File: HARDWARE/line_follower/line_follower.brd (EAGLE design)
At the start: 150 x 110.3 mm, 67 parts, among them IC1 ATMEGA328PMA, IC2 LF50, IC3 L6205, IC4 L3GD20HSMD, Q1 CSM-7X-DU, T1 BPX81, T2 BPX81, T3 BPX81, T4 BPX81, T7 BPX81, T8 BPX81

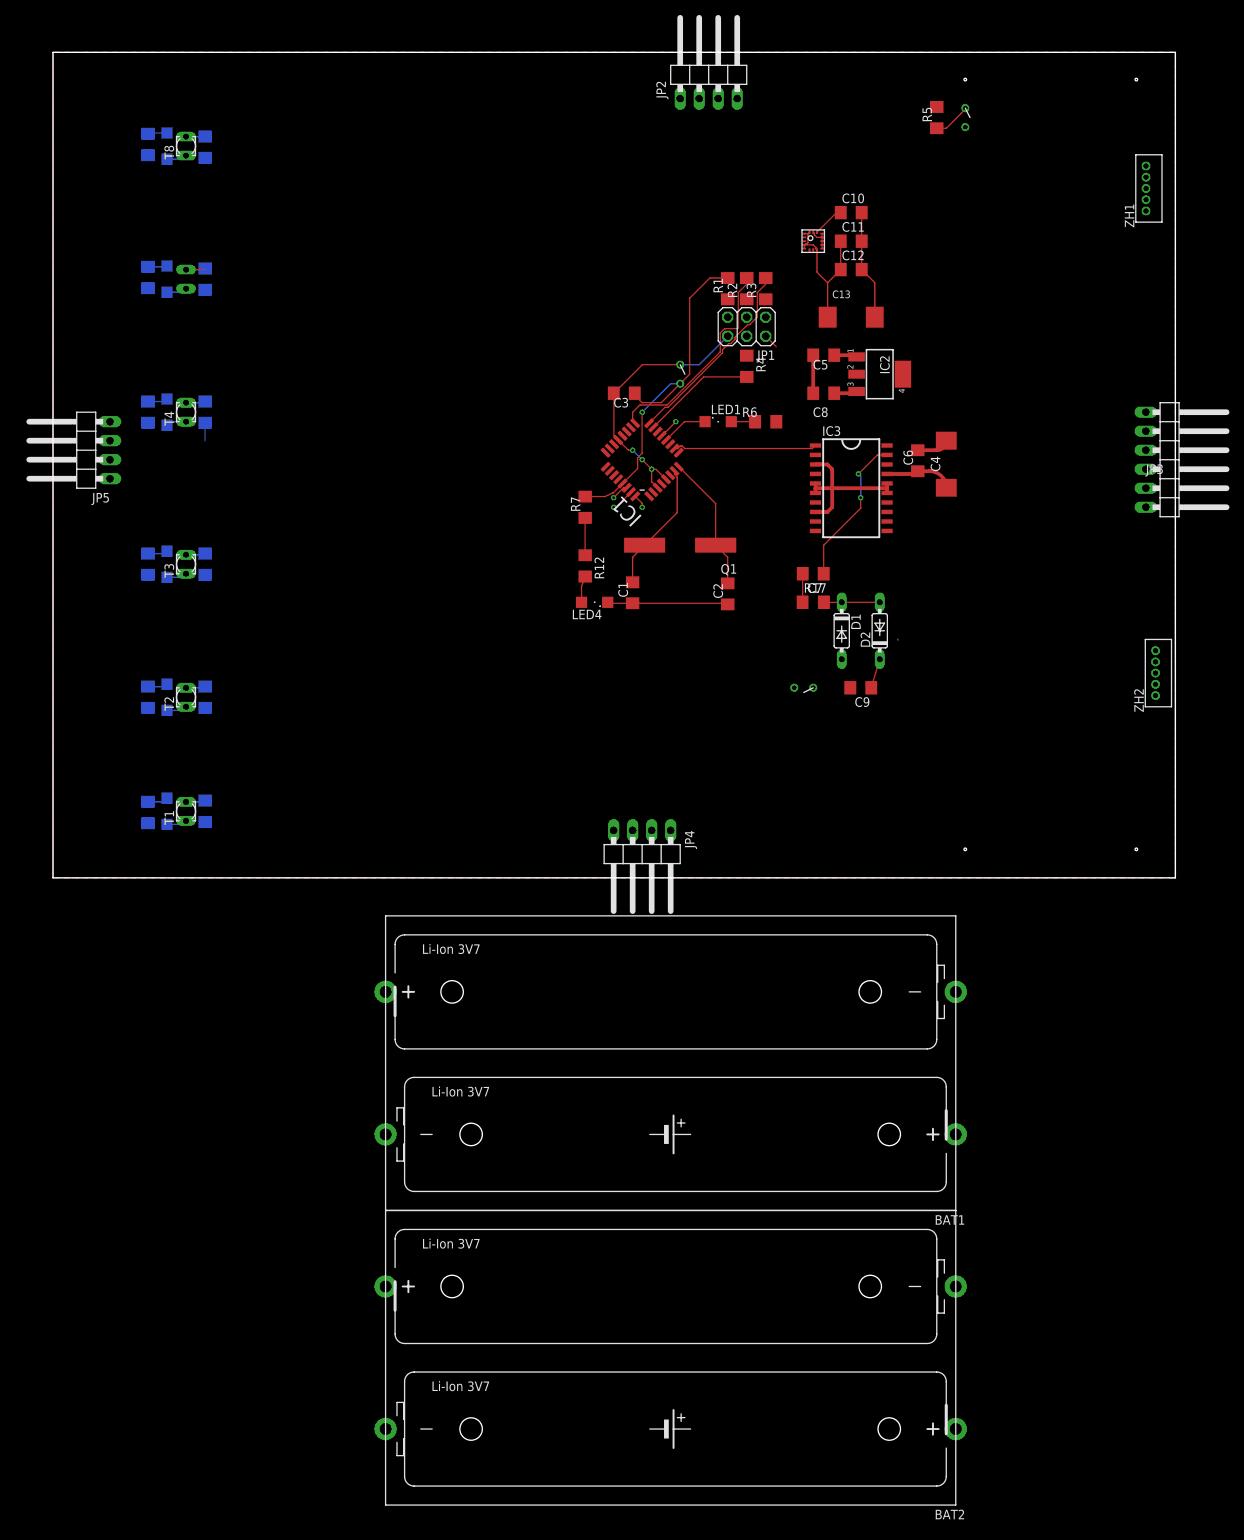
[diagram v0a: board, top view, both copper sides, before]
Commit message: finished front module
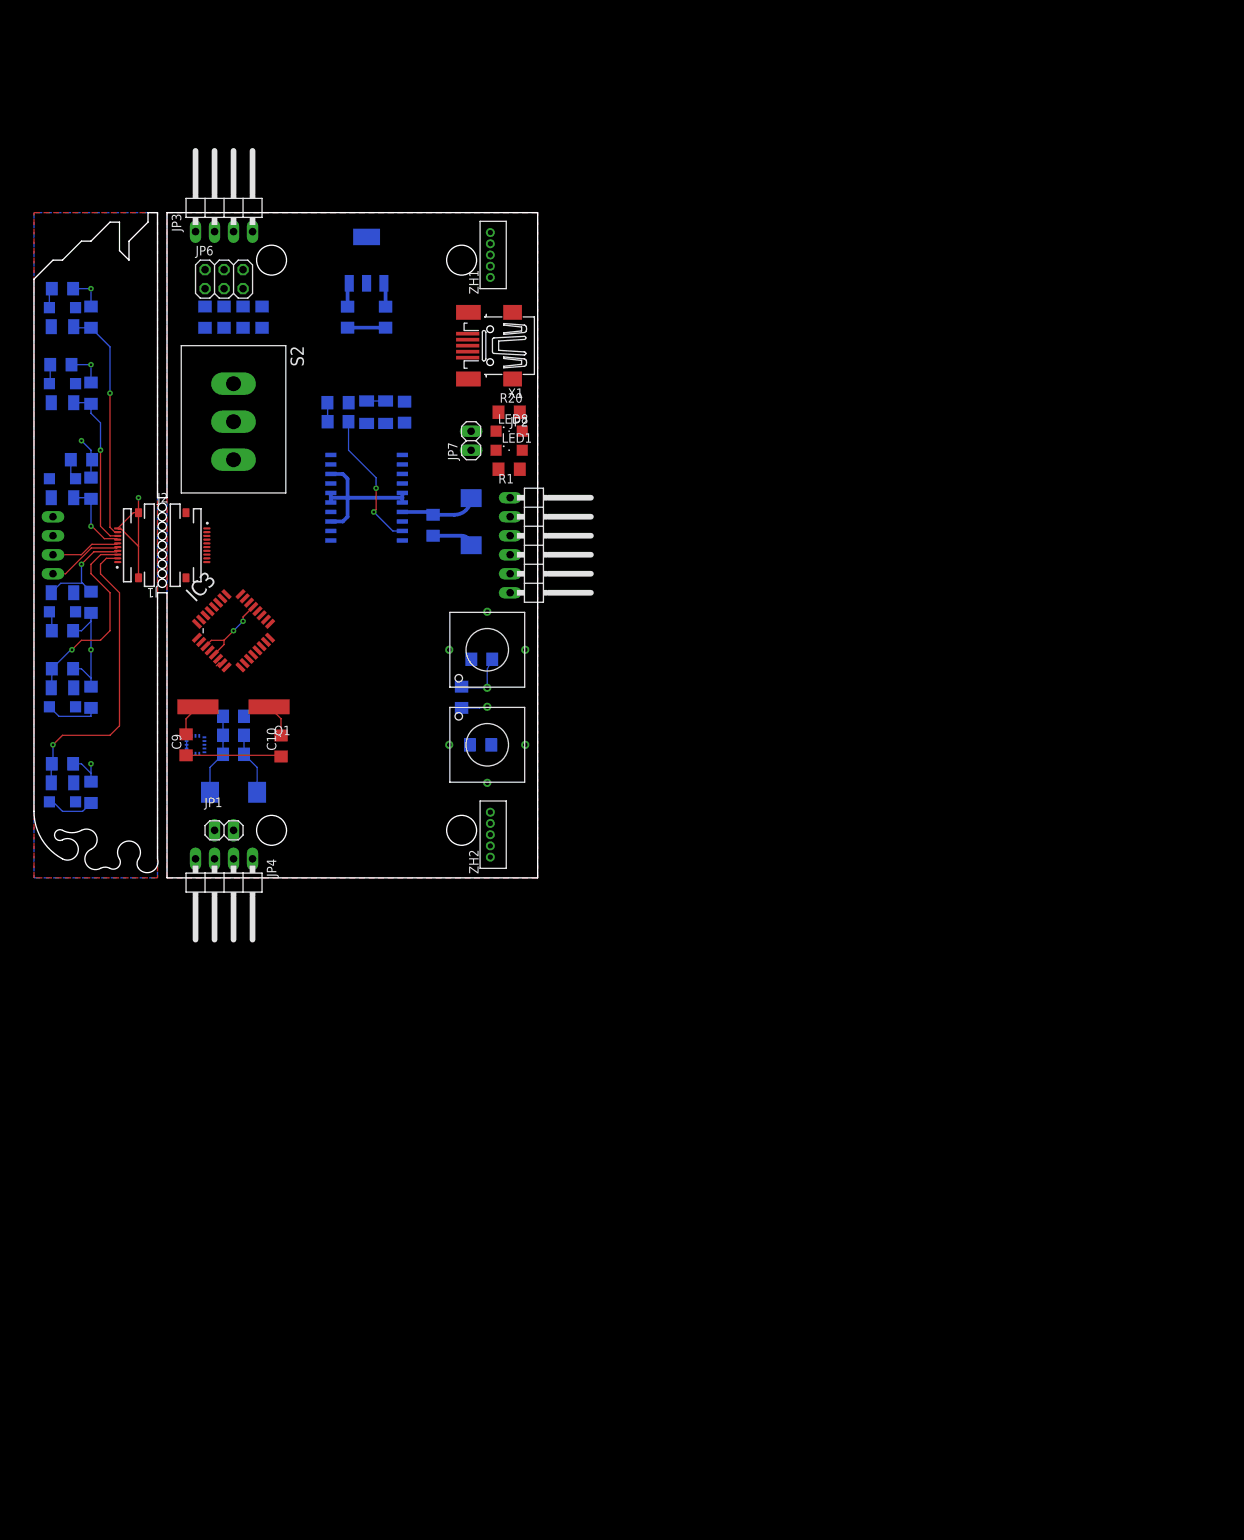
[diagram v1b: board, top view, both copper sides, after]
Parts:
- removed BAT1, BAT2: BATSERIES, martinmake:BAT2X18650SERIES
- removed LED10, LED9: White, led:SML1206
- removed R22, R24: 220, rcl:R1206
- removed R23, R25: 10k, rcl:R1206
- removed T7, T8: BPX81, opto-trans-siemens:BPX81
- removed USR: SWITCHTHT, martinmake:SWITCH
- added J1, J2: FFC2B05-10-X_REVC, FFC2B05-10-X_REVC:GCT_FFC2B05-10-X_REVC
- added JP6: ICSP, pinhead:2X03
- added JP7: 3S/4S, pinhead:1X02
- added LED7: White, led:SML1206
- added LED8: Orange, led:SML1206
- added R18, R19: 120, rcl:R1206
- added R20: 220, rcl:R1206
- added R21: 100k, rcl:R1206
- added S1: BUTTON, martinmake:BUTTON
- added T5, T6: ELPT15-21C, martinmake:1206
- added X1: MINI-USB-SCHIELD-32005-201, con-cypressindustries:32005-201
- C1: value 22p -> 10u; device rcl:C1206 -> rcl:SMC_D
- C10, C9: value 10n -> 22p
- C13: value 10u -> 100n; device rcl:SMC_D -> rcl:C1206
- C2: value 22p -> 100n
- C4: value 100u -> 10n; device rcl:SMC_D -> rcl:C1206
- C5: value 100n -> 100u; device rcl:C1206 -> rcl:SMC_D
- C8: value 100n -> 10n
- D1, D2: device diode:DO35-7 -> martinmake:1206
- IC1: value ATMEGA328PMA -> L3GD20HSMD; device martinmake:TQFP32 -> martinmake:LGA-16
- IC2: value LF50 -> L6205; device linear:SOT223 -> martinmake:SO20
- IC3: value L6205 -> ATMEGA328PMA; device martinmake:SO20 -> martinmake:TQFP32
- IC4: value L3GD20HSMD -> LF33; device martinmake:LGA-16 -> linear:SOT223
- JP1: value ICSP -> (none); device pinhead:2X03 -> pinhead:1X02
- JP2: value RDS -> UART; device pinhead:1X04/90 -> pinhead:1X06/90
- JP3: value UART -> RDS; device pinhead:1X06/90 -> pinhead:1X04/90
- LED4: value Orange -> White
- Q1: value CSM-7X-DU -> 10MHz
- R1: value 120 -> 680
- R13, R15: value 220 -> 10k
- R14: value 10k -> 220
- R16: value 10k -> 120
- R17: value 220 -> 120
- R2: value 120 -> 1k
- R3, R4: value 120 -> 220
- R5: value 1k -> 10k
- R6: value 680 -> 220
- R7: value 100k -> 10k
- S2: value SWITCHTHT -> DUALSWITCH; device martinmake:SWITCH -> martinmake:DUALSWITCH
- S3: value SWITCHTHT -> BUTTON; device martinmake:SWITCH -> martinmake:BUTTON
- T1, T2, T3, T4: value BPX81 -> ELPT15-21C; device opto-trans-siemens:BPX81 -> martinmake:1206
- moved R5 145.3 mm to (1.27, 15.2), flipped to the bottom, turned to 0 degrees
- moved JP3 131.5 mm to (22.9, 90.2), turned to 0 degrees
- moved R4 104.5 mm to (5.08, 11.4), flipped to the bottom
- moved C10 104.3 mm to (30.5, 17.6), turned to 90 degrees
- moved C4 101.0 mm to (24.1, 21.6), flipped to the bottom, turned to 0 degrees
- moved R6 97.4 mm to (5.08, 24.1), flipped to the bottom, turned to 270 degrees
- moved JP1 97.0 mm to (22.9, 6.35), turned to 0 degrees
- moved ZH2 91.5 mm to (57.1, 1.27)
- moved C9 90.5 mm to (17.8, 17.8), turned to 90 degrees
- moved ZH1 88.1 mm to (57.1, 78.7)
- moved R17 87.5 mm to (22.9, 74.9), flipped to the bottom, turned to 270 degrees
- moved IC3 84.7 mm to (24.1, 33.0), turned to 45 degrees
- moved R12 75.1 mm to (1.05, 68.6), flipped to the bottom, turned to 0 degrees
- moved R7 73.1 mm to (1.27, 27.9), flipped to the bottom, turned to 0 degrees
- moved D2 72.2 mm to (44.5, 62.2), flipped to the bottom, turned to 270 degrees
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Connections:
- removed net GND2: LED10.C, LED2.C, LED3.C, LED5.C, LED6.C, LED9.C, T1.E, T2.E, T3.E, T4.E, T7.E, T8.E
- removed net N$10: BAT1.+@1, BAT1.-@2
- removed net N$11: IC4.6
- removed net N$13: IC4.7
- removed net N$14: BAT1.+@2, S3.P$2
- removed net N$15: BAT1.-@1, BAT2.+@2
- removed net N$24: R15.1
- removed net N$32: R13.1
- removed net N$38: R22.1
- removed net N$40: R10.1
- removed net N$41: R24.1
- removed net N$45: R8.1
- removed net VM: C4.+, C5.1, C6.1, C9.2, D1.A, IC2.1, IC3.14, IC3.17, S3.P$1
- new net F_ADC0: J1.2, R5.2, T1.1
- new net F_ADC1: J1.3, R7.2, T2.1
- new net F_ADC2: J1.4, R9.2, T3.1
- new net F_ADC3: J1.7, R11.2, T4.1
- new net F_ADC6: J1.8, R13.2, T5.1
- new net F_ADC7: J1.9, R15.2, T6.1
- new net F_GND: J1.10, J1.11, J1.12, JP5.2, LED2.C, LED3.C, LED4.C, LED5.C, LED6.C, LED7.C, T1.2, T2.2, T3.2, T4.2, T5.2, T6.2
- new net F_SCL: J1.5, JP5.4
- new net F_SDA: J1.6, JP5.3
- new net F_VCC: J1.1, JP5.1, R10.1, R11.1, R12.1, R13.1, R14.1, R15.1, R4.1, R5.1, R6.1, R7.1, R8.1, R9.1
- new net N$8: IC1.7, JP1.1
- new net VB: C11.1, C5.+, C6.1, C7.2, D1.1, IC2.14, IC2.17, IC4.1, JP7.1, S2.A, S2.COM
- new net VUSB: S2.B, X1.1
- net !RESET: now also C13.1, IC3.29, R16.2, R21.2, S3.A@1, S3.A@2; no longer C3.1, IC1.29, R1.2, R7.2, S2.P$2
- net !SS: now also IC3.14; no longer IC1.14
- net ADC0: now also IC3.23, J2.2; no longer IC1.23, R9.2, T1.C
- net ADC1: now also IC3.24, J2.3; no longer IC1.24, R11.2, T2.C
- net ADC2: now also IC3.25, J2.4; no longer IC1.25, R14.2, T3.C
- net ADC3: now also IC3.26, J2.7; no longer IC1.26, R16.2, T4.C
- net ADC6: now also IC3.19, J2.8; no longer IC1.19, R23.2, T7.C
- net ADC7: now also IC3.22, J2.9; no longer IC1.22, R25.2, T8.C
- net DIRA: now also IC2.2; no longer IC1.2
- net DIRB: now also IC2.10, IC3.11; no longer IC1.11, IC3.10
- net GND: now also C1.-, C10.1, C13.2, C2.2, C4.2, C5.-, C9.1, IC1.10, IC1.11, IC1.12, IC1.13, IC1.15, IC1.9, IC2.15, IC2.16, IC2.3, IC2.5, IC2.6, IC2.8, IC3.21, IC4.4, J2.10, J2.11, J2.12, JP2.1, JP3.2, JP6.6, JP7.2, LED8.C, R2.2, S3.B@1, S3.B@2, X1.5, X1.M1, X1.M2, X1.M3, X1.M4; no longer BAT2.-@1, C1.1, C10.2, C13.-, C2.1, C4.-, C5.2, C8.2, IC1.21, IC1.3, IC1.5, IC2.4, IC3.15, IC3.16, IC3.6, IC3.8, IC4.10, IC4.11, IC4.12, IC4.13, IC4.15, IC4.9, JP1.6, JP2.2, JP3.1, JP5.2, LED4.C, R5.2, S2.P$1
- net INT0: now also IC3.32; no longer IC1.32
- net INT1: now also IC3.1; no longer IC1.1
- net LED: now also IC3.12; no longer IC1.12
- net MISO: now also IC3.16, R18.2; no longer IC1.16, R3.2
- net MOSI: now also IC3.15, R19.2; no longer IC1.15, R4.2
- net N$1: now also LED4.A, R8.2; no longer LED5.A, R13.2
- net N$12: now also LED5.A, R10.2; no longer LED6.A, R15.2
- net N$2: now also C7.1, D2.2, IC2.12; no longer C9.1, D2.C, IC3.12
- net N$22: now also LED7.A, R14.2; no longer LED10.A, R24.2
- net N$3: now also D1.2, D2.1, R3.2; no longer D1.C, D2.A, R17.2
- net N$30: now also LED6.A, R12.2; no longer LED9.A, R22.2
- net N$33: now also JP6.1, R18.1; no longer JP1.1, R3.1
- net N$36: now also LED8.A, R20.2; no longer LED4.A, R12.2
- net N$4: now also C8.2, R3.1; no longer C7.2, R17.1
- net N$43: now also R6.2; no longer R10.2
- net N$47: now also R4.2; no longer R8.2
- net N$49: now also JP6.3, R17.1; no longer JP1.3, R2.1
- net N$5: now also R1.1; no longer R6.1
- net N$50: now also JP6.5, R16.1; no longer JP1.5, R1.1
- net N$51: now also JP6.4, R19.1; no longer JP1.4, R4.1
- net N$6: now also C4.1, IC1.14; no longer C10.1, IC4.14
- net N$7: now also C8.1, IC2.19; no longer C7.1, IC3.19
- net N$9: now also IC1.6, JP1.2; no longer BAT2.+@1, BAT2.-@2
- net OC0A: now also IC2.1, IC3.10; no longer IC1.10, IC3.1
- net OC0B: now also IC2.9; no longer IC1.9
- net OUT1A: now also IC2.4; no longer IC3.4
- net OUT1B: now also IC2.7; no longer IC3.7
- net OUT2A: now also IC2.18; no longer IC3.18
- net OUT2B: now also IC2.13; no longer IC3.13
- net RX: now also IC3.30, JP2.4; no longer IC1.30, JP3.4
- net SCK: now also IC3.17, R17.2; no longer IC1.17, R2.2
- net SCL: now also IC1.2, IC3.28, J2.5, JP3.4; no longer IC1.28, IC4.2, JP2.3, JP5.4
- net SDA: now also IC1.3, IC3.27, J2.6, JP3.3; no longer IC1.27, IC4.3, JP2.4, JP5.3
- net TX: now also IC3.31, JP2.5; no longer IC1.31, JP3.5
- net USR: now also IC3.13, R2.1, S1.A@1, S1.A@2; no longer IC1.13, R5.1, USR.P$1
- net VCC: now also C1.+, C2.1, C3.1, IC1.1, IC1.16, IC1.5, IC1.8, IC2.11, IC2.20, IC3.18, IC3.4, IC3.6, IC4.3, J2.1, JP2.3, JP3.1, JP6.2, R1.2, R20.1, R21.1, S1.B@1, S1.B@2; no longer C11.1, C13.+, C8.1, IC1.18, IC1.20, IC1.6, IC2.3, IC3.11, IC4.1, IC4.16, IC4.4, IC4.5, IC4.8, JP1.2, JP2.1, JP3.3, JP5.1, R11.1, R12.1, R14.1, R16.1, R23.1, R25.1, R6.2, R7.1, R9.1, USR.P$2
- net XTAL1: now also C9.2, IC3.7; no longer C1.2, IC1.7
- net XTAL2: now also C10.2, IC3.8; no longer C2.2, IC1.8
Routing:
- net !RESET: track 48.9 -> 7.46 mm, vias 1 -> 0
- net F_ADC0: track 0.00 -> 40.4 mm, vias 0 -> 1
- net F_VCC: track 0.00 -> 36.4 mm, vias 0 -> 5
- net F_ADC7: track 0.00 -> 31.4 mm, vias 0 -> 1
- net GND: track 102.3 -> 71.1 mm, vias 3 -> 2
- net SCK: track 29.5 -> 0.00 mm
- net F_ADC1: track 0.00 -> 26.5 mm, vias 0 -> 1
- net MISO: track 26.4 -> 0.00 mm
- net F_ADC6: track 0.00 -> 22.1 mm, vias 0 -> 1
- net OC0A: track 19.3 -> 0.00 mm
- net VCC: track 33.8 -> 15.0 mm
- net F_GND: track 0.00 -> 18.6 mm, vias 0 -> 1
- net GND2: track 16.4 -> 0.00 mm
- net MOSI: track 15.3 -> 0.00 mm
- net F_ADC2: track 0.00 -> 14.5 mm, vias 0 -> 1
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- added copper zone on layer 16, net F_GND
- added copper zone on layer 1, net F_VCC
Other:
- board size 150 x 110.3 mm -> 67.3 x 88.9 mm

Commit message: finished PCB
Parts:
- moved ZH1 77.6 mm to (62.2, 1.27)
- moved ZH2 77.6 mm to (62.2, 78.7)
- moved C5 18.2 mm to (45.1, 33.0), turned to 0 degrees
- moved C6 11.0 mm to (44.6, 38.1), turned to 0 degrees
- moved C9 8.89 mm to (26.7, 17.8)
- moved R2 5.24 mm to (62.2, 19.1), turned to 90 degrees
- moved C1 5.08 mm to (29.2, 11.4), flipped to the top, turned to 180 degrees
- moved C8 4.58 mm to (40.6, 57.1)
- moved R3 4.58 mm to (40.6, 59.7)
- moved D1 4.58 mm to (44.5, 58.4)
- moved IC2 4.58 mm to (44.5, 47.0)
- moved C7 4.58 mm to (49.5, 58.4)
- moved D2 4.58 mm to (47.0, 58.4)
- moved C13 4.02 mm to (61.1, 30.5)
- moved JP6 4.02 mm to (26.7, 81.3)
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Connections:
- new net N$10: C11.1, IC4.1, S2.COM
- net VB: no longer C11.1, IC4.1, S2.COM
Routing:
- net VCC: track 15.0 -> 143.7 mm, vias 0 -> 6
- net !RESET: track 7.46 -> 124.6 mm, vias 0 -> 5
- net INT1: track 0.14 -> 111.8 mm, vias 0 -> 1
- net SCL: track 0.00 -> 101.5 mm, vias 0 -> 3
- net SDA: track 0.00 -> 98.2 mm, vias 0 -> 4
- net TX: track 0.00 -> 72.1 mm, vias 0 -> 2
- net RX: track 0.00 -> 63.9 mm, vias 0 -> 6
- net LED: track 0.00 -> 59.4 mm, vias 0 -> 2
- net INT0: track 0.00 -> 58.3 mm, vias 0 -> 1
- net VB: track 13.5 -> 70.5 mm, vias 0 -> 1
- net OUT1A: track 0.00 -> 56.6 mm, vias 0 -> 1
- net SCK: track 0.00 -> 50.4 mm, vias 0 -> 3
- net OUT2A: track 0.00 -> 50.0 mm, vias 0 -> 1
- net OUT1B: track 0.00 -> 49.8 mm
- net MISO: track 0.00 -> 45.3 mm, vias 0 -> 3
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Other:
- board size 67.3 x 88.9 mm -> 68.6 x 88.9 mm

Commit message: common
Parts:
- moved C13 2.24 mm to (63.3, 30.5), turned to 180 degrees
- turned C2 to 180 degrees
- turned C3 to 180 degrees
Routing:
- net GND: track 110.9 -> 148.6 mm, vias 4 -> 8
- net OUT1A: track 56.6 -> 53.5 mm, vias 1 -> 2
- net N$10: track 36.3 -> 38.8 mm
- net N$2: track 6.59 -> 8.91 mm
- net VCC: track 143.7 -> 141.3 mm
- net INT1: track 111.8 -> 109.9 mm
- net LED: track 59.4 -> 58.0 mm
- net OUT2A: track 50.0 -> 48.9 mm
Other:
- outline, holes or cut-outs redrawn

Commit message: common
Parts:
- added C14, C15: 100u, rcl:UD-6,3X5,8_NICHICON
- added C16: 100n, rcl:C1206
- C1: value 10u -> 100u; device rcl:SMC_D -> rcl:UD-6,3X5,8_NICHICON
- C10, C9: value 22p -> 100n
- C12, C13: value 100n -> 22p
- C5: device rcl:SMC_D -> rcl:UD-6,3X5,8_NICHICON
- IC4: device linear:SOT223 -> linear:TO220H
- JP7: value 3S/4S -> 3S
- R10, R12, R14, R4, R6, R8: value 220 -> 120
- R20: value 220 -> 470
- X1: value MINI-USB-SCHIELD-32005-201 -> MINI-USB-SCHIELD-32005-301; device con-cypressindustries:32005-201 -> con-cypressindustries:32005-301
- moved IC4 73.8 mm to (41.9, 8.89), flipped to the top, turned to 180 degrees
- moved JP2 62.8 mm to (13.8, 14.0), turned to 90 degrees
- moved C11 59.1 mm to (20.3, 22.9), flipped to the top, turned to 0 degrees
- moved JP1 58.0 mm to (15.2, 63.5), turned to 270 degrees
- moved C1 57.2 mm to (27.9, 68.6)
- moved JP7 53.6 mm to (64.8, 5.08), turned to 270 degrees
- moved S1 53.3 mm to (61.0, 71.1), turned to 90 degrees
- moved S2 53.2 mm to (61.0, 20.3)
- moved R2 52.1 mm to (62.2, 71.1), turned to 180 degrees
- moved R21 46.7 mm to (24.1, 55.9), turned to 0 degrees
- moved IC1 45.7 mm to (22.9, 63.5), turned to 90 degrees
- moved C12 45.4 mm to (22.9, 34.3)
- moved C4 44.5 mm to (29.2, 66.0)
- moved C2 44.5 mm to (29.2, 61.0)
- moved C3 44.5 mm to (29.2, 63.5)
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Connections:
- new net V+: X1.1
- net !RESET: now also C16.1; no longer C13.1
- net GND: now also C10.2, C12.1, C13.1, C14.-, C15.-, C16.2, C9.2, IC4.2; no longer C10.1, C12.2, C13.2, C9.1, IC4.4
- net N$10: now also C14.+; no longer C11.1
- net VCC: now also C10.1, C11.1, C15.+, C9.1; no longer C12.1
- net VUSB: no longer X1.1
- net XTAL1: now also C12.2; no longer C9.2
- net XTAL2: now also C13.2; no longer C10.2
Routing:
- net VCC: track 141.3 -> 44.2 mm, vias 6 -> 3
- net !RESET: track 124.1 -> 52.8 mm, vias 5 -> 2
- net TX: track 72.1 -> 26.5 mm, vias 2 -> 1
- net INT1: track 109.9 -> 66.5 mm
- net RX: track 63.9 -> 28.1 mm, vias 6 -> 1
- net VUSB: track 34.0 -> 0.00 mm
- net DIRA: track 43.7 -> 10.8 mm, vias 3 -> 1
- net OC0B: track 29.6 -> 8.30 mm
- net DIRB: track 29.2 -> 9.49 mm
- net SCK: track 50.4 -> 33.5 mm, vias 3 -> 1
- net MOSI: track 44.7 -> 29.5 mm, vias 3 -> 1
- net SDA: track 98.2 -> 113.1 mm, vias 4 -> 2
- net GND: track 148.6 -> 133.9 mm, vias 8 -> 3
- net LED: track 58.0 -> 45.3 mm, vias 2 -> 0
- net N$10: track 38.8 -> 27.8 mm
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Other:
- board size 68.6 x 88.9 mm -> 73.7 x 88.9 mm

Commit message: common
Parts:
- added LED9: Orange, led:SML1206
- JP2: device pinhead:1X06/90 -> pinhead:1X06
- LED2: value White -> Purple
- LED8: value Orange -> White
- R2: value 1k -> 680
- moved LED2 98.8 mm to (76.5, 71.1), flipped to the top
- moved JP6 70.7 mm to (38.7, 12.7), turned to 180 degrees
- moved R19 68.4 mm to (40.0, 8.88), turned to 180 degrees
- moved R18 61.3 mm to (41.3, 17.8), turned to 90 degrees
- moved R17 59.7 mm to (38.7, 17.8), turned to 90 degrees
- moved R16 58.4 mm to (36.2, 17.8), turned to 90 degrees
- moved LED8 57.5 mm to (10.5, 78.7), flipped to the bottom
- moved R20 53.1 mm to (37.8, 16.5), turned to 180 degrees
- moved R3 33.9 mm to (72.7, 53.3), turned to 90 degrees
- moved C8 32.1 mm to (70.2, 48.2), turned to 180 degrees
- moved C11 31.8 mm to (33.1, 52.0), turned to 225 degrees
- moved C9 29.6 mm to (46.0, 42.5), turned to 270 degrees
- moved D1 27.2 mm to (70.2, 53.3), turned to 90 degrees
- moved C14 25.7 mm to (81.6, 33.0)
- moved C10 25.6 mm to (42.9, 37.5), turned to 135 degrees
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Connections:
- removed net !SS: IC3.14
- removed net LED: IC3.12, LED1.C
- removed net V+: X1.1
- new net LEDA: IC3.13, LED2.C
- new net LEDB: IC3.14, LED1.C
- new net N$13: LED2.A, R2.1
- net ADC0: now also J2.4; no longer J2.2
- net ADC1: now also J2.5; no longer J2.3
- net ADC2: now also J2.6; no longer J2.4
- net ADC6: now also J2.2; no longer J2.8
- net ADC7: now also J2.3; no longer J2.9
- net F_ADC0: now also J1.7; no longer J1.2
- net F_ADC1: now also J1.6; no longer J1.3
- net F_ADC2: now also J1.5; no longer J1.4
- net F_ADC3: now also J1.4; no longer J1.7
- net F_ADC6: now also J1.9; no longer J1.8
- net F_ADC7: now also J1.8; no longer J1.9
- net F_GND: now also J1.1, LED8.C; no longer J1.10, LED2.C
- net F_SCL: now also J1.2; no longer J1.5
- net F_SDA: now also J1.3; no longer J1.6
- net F_VCC: now also J1.10; no longer J1.1
- net GND: now also LED9.C, S1.B@1, S1.B@2; no longer LED8.C, R2.2
- net N$1: now also LED5.A; no longer LED4.A
- net N$12: now also LED6.A; no longer LED5.A
- net N$22: now also LED8.A; no longer LED7.A
- net N$30: now also LED7.A; no longer LED6.A
- net N$36: now also LED9.A; no longer LED8.A
- net N$43: now also LED4.A; no longer LED3.A
- net N$47: now also LED3.A; no longer LED2.A
- net SCL: now also J2.9; no longer J2.5
- net SDA: now also J2.8; no longer J2.6
- net USR: now also IC3.12; no longer IC3.13, R2.1
- net VCC: now also R2.2; no longer S1.B@1, S1.B@2
- net VUSB: now also X1.1
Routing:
- net LEDB: track 0.00 -> 46.1 mm
- net LED: track 45.3 -> 0.00 mm
- net LEDA: track 0.00 -> 44.7 mm
- net VUSB: track 0.00 -> 32.5 mm
- net GND: track 133.9 -> 119.1 mm, vias 3 -> 8
- net INT0: track 48.6 -> 62.8 mm, vias 1 -> 0
- net MOSI: track 29.5 -> 43.2 mm
- net SDA: track 113.1 -> 100.6 mm
- net VCC: track 44.2 -> 32.2 mm, vias 3 -> 4
- net N$10: track 27.8 -> 35.4 mm
- net ADC6: track 14.2 -> 6.72 mm, vias 2 -> 0
- net DIRA: track 10.8 -> 17.1 mm
- net F_VCC: track 36.3 -> 30.2 mm, vias 5 -> 6
- net F_SDA: track 9.28 -> 15.3 mm
- net F_SCL: track 10.1 -> 16.2 mm
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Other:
- board size 73.7 x 88.9 mm -> 85.4 x 88.9 mm
- board text added: "/home/arch/Documents/proj/slate_vixen/HARDWARE/line_follower/printing/dragon_head.bmp"
